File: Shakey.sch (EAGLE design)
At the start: 38 parts, among them CN1 CONN_USB-4UCON-11071, Y1 16Mhz

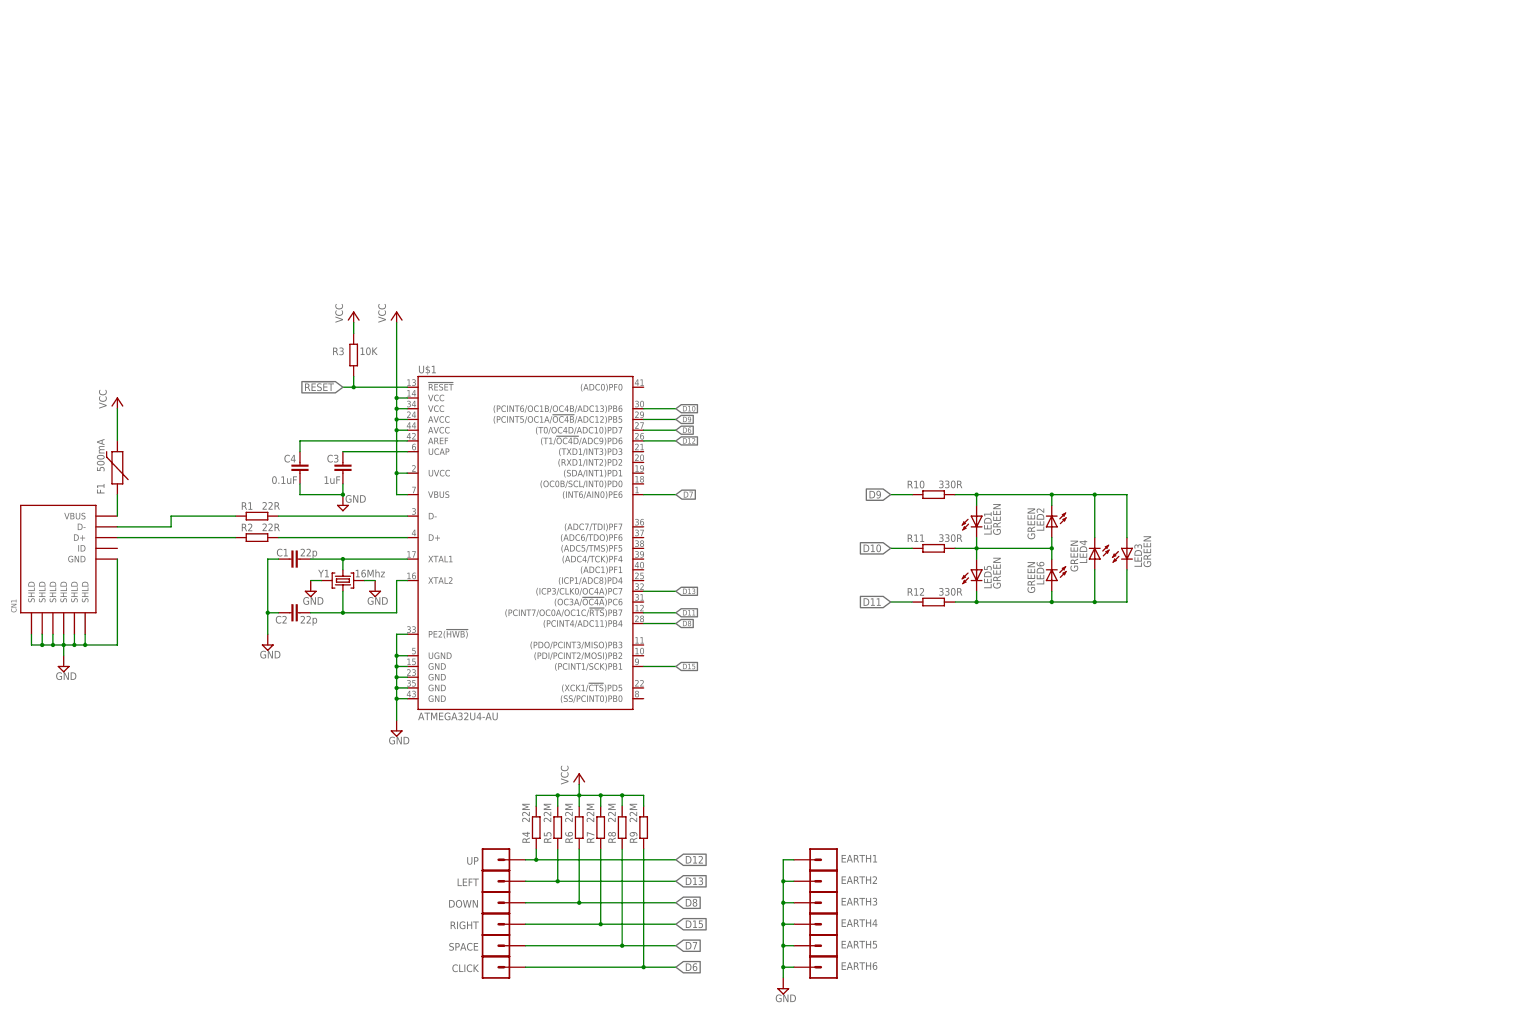
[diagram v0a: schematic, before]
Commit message: completed basic schematic
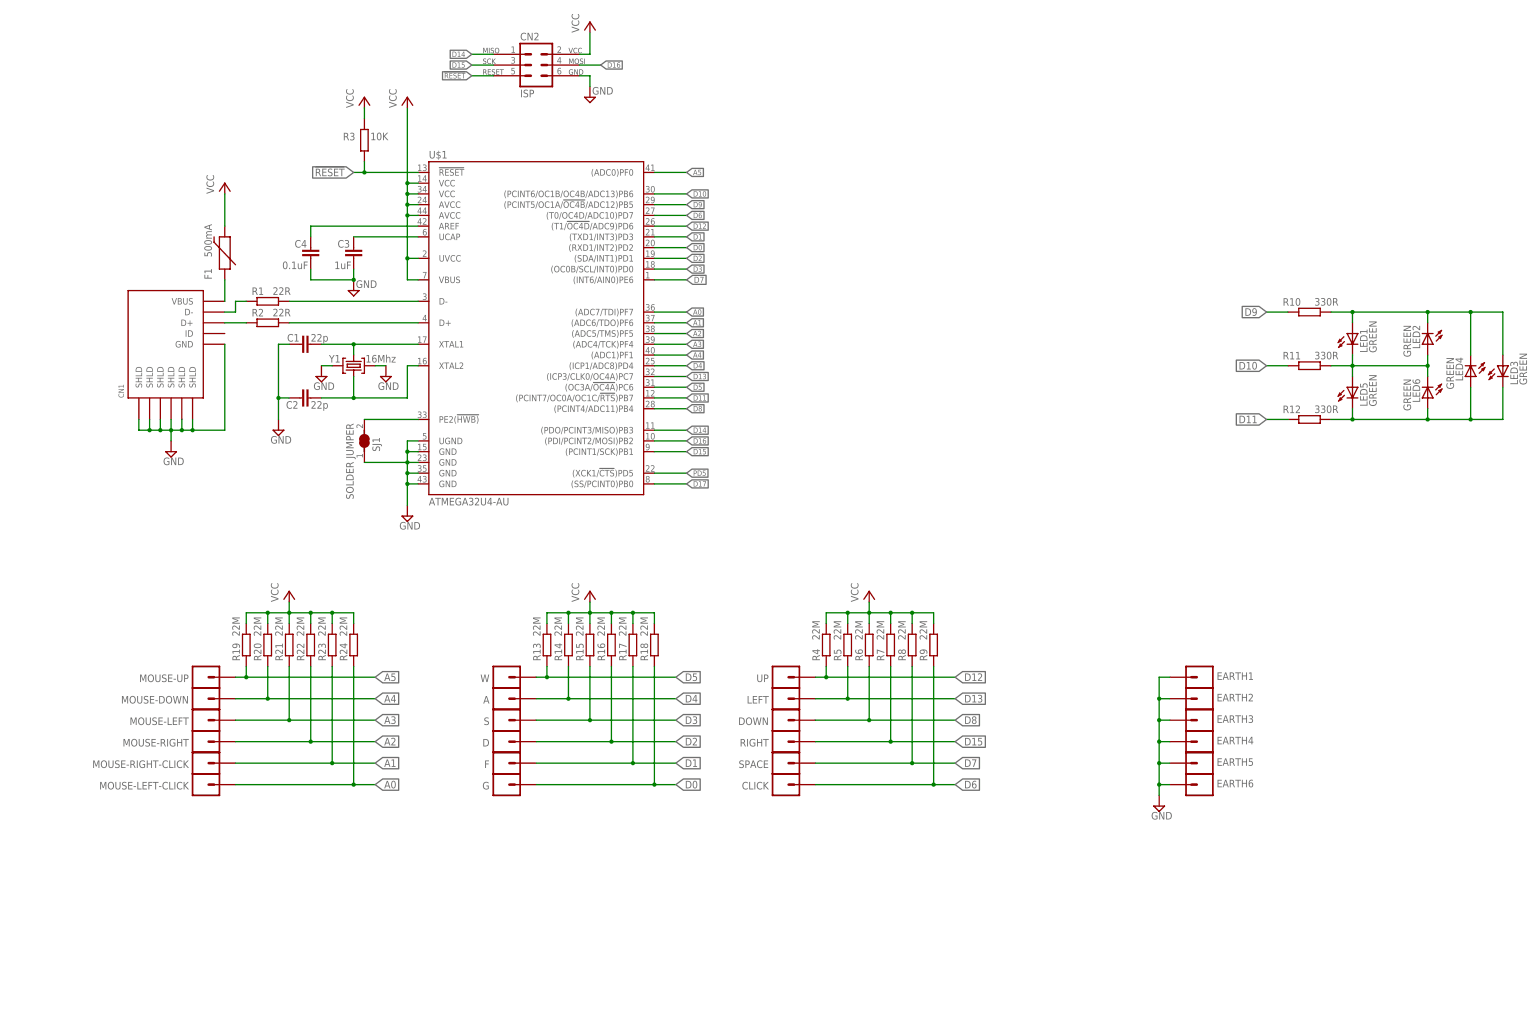
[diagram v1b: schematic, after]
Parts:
- added A, D, F, G, MOUSE-DOWN, MOUSE-LEFT, MOUSE-LEFT-CLICK, MOUSE-RIGHT, MOUSE-RIGHT-CLICK, MOUSE-UP, S, W: MA01-1-ALLIGATOR-3MM, SixthLogic:MA01-1-ALLIGATOR-3MM
- added CN2: ISP, SixthLogic:DEBUGPORT-6PIN-ISP-AVR
- added R13, R14, R15, R16, R17, R18, R19, R20, R21, R22, R23, R24: 22M, rcl:R-EU_R0603
- added SJ1: SOLDER JUMPER, SixthLogic:SOLDER_JUMPER_NC
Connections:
- new net A0: MOUSE-LEFT-CLICK.1, R24.1, U$1.(ADC7/TDI)PF7
- new net A1: MOUSE-RIGHT-CLICK.1, R23.1, U$1.(ADC6/TDO)PF6
- new net A2: MOUSE-RIGHT.1, R22.1, U$1.(ADC5/TMS)PF5
- new net A3: MOUSE-LEFT.1, R21.1, U$1.(ADC4/TCK)PF4
- new net A4: MOUSE-DOWN.1, R20.1, U$1.(ADC1)PF1
- new net A5: MOUSE-UP.1, R19.1, U$1.(ADC0)PF0
- new net D0: G.1, R18.1, U$1.(RXD1/INT2)PD2
- new net D1: F.1, R17.1, U$1.(TXD1/INT3)PD3
- new net D14: CN2.1, U$1.(PDO/PCINT3/MISO)PB3
- new net D16: CN2.4, U$1.(PDI/PCINT2/MOSI)PB2
- new net D17: U$1.(SS/PCINT0)PB0
- new net D2: D.1, R16.1, U$1.(SDA/INT1)PD1
- new net D3: R15.1, S.1, U$1.(OC0B/SCL/INT0)PD0
- new net D4: A.1, R14.1, U$1.(ICP1/ADC8)PD4
- new net D5: R13.1, U$1.(OC3A/!OC4A!)PC6, W.1
- new net N$13: SJ1.2, U$1.PE2(!HWB)
- new net PD5: U$1.(XCK1/!CTS!)PD5
- net !RESET!: now also CN2.5
- net D15: now also CN2.3
- net GND: now also CN2.6, SJ1.1; no longer U$1.PE2(!HWB)
- net VCC: now also CN2.2, R13.2, R14.2, R15.2, R16.2, R17.2, R18.2, R19.2, R20.2, R21.2, R22.2, R23.2, R24.2
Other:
- moved on the sheet: C1, C2, C3, C4, CLICK, CN1, DOWN, EARTH1, EARTH2, EARTH3, EARTH4, EARTH5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

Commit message: completed schematic
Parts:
- removed D, S: MA01-1-ALLIGATOR-3MM, SixthLogic:MA01-1-ALLIGATOR-3MM
- removed U$1: ATMEGA32U4-AU, SixthLogic:ATMEGA32U4-AU
- added C5, C8: 1uF, rcl:C-EUC0603
- added C6: 0.1uF, rcl:C-EUC0603
- added C7: 2.2uF, rcl:C-EUC0603
- added C9: 0.47uF, rcl:C-EUC0603
- added LED7, LED8: YELLOW, led:LEDCHIPLED_0603
- added LED9: RED, led:LEDCHIPLED_0603
- added PC1: 10uF, SixthLogic:CAP_POL-CT6032
- added R25, R26, R27: 1K, rcl:R-EU_R0603
- added R28, R29, R30, R31: 10K, rcl:R-EU_R0603
- added TR1, TR2: BSS138, SixthLogic:MOSFET-N-BSS138
- added U1: ATMEGA32U4-AU, SixthLogic:ATMEGA32U4-AU
- added U2: ICM-20689, SixthLogic:ICM-20689
- added U3: AP2210K-3.3TRG1, SixthLogic:AP2210K-3.3TRG1
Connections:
- removed net D17: U$1.(SS/PCINT0)PB0
- removed net D2: D.1, R16.1, U$1.(SDA/INT1)PD1
- removed net D3: R15.1, S.1, U$1.(OC0B/SCL/INT0)PD0
- removed net PD5: U$1.(XCK1/!CTS!)PD5
- new net 3.3V: C5.2, C6.2, C7.2, R28.2, R29.2, TR1.G, TR2.G, U2.NCS, U2.VDD, U2.VDDIO, U3.VOUT
- new net HWB: SJ1.2, U1.PE2(!HWB)
- new net N$17: LED7.A, R25.1
- new net N$18: LED8.A, R26.1
- new net N$19: LED9.A, R27.1
- new net RX_LED: LED8.C, U1.(SS/PCINT0)PB0
- new net SCL_HV: R31.1, TR2.D, U1.(OC0B/SCL/INT0)PD0
- new net SCL_LV: R29.1, TR2.S, U2.SCL/SCLK
- new net SDA_HV: R30.1, TR1.D, U1.(SDA/INT1)PD1
- new net SDA_LV: R28.1, TR1.S, U2.SDA/SDI
- new net TX_LED: LED7.C, U1.(XCK1/!CTS!)PD5
- net !RESET!: now also U1.!RESET; no longer U$1.!RESET
- net A0: now also U1.(ADC7/TDI)PF7; no longer U$1.(ADC7/TDI)PF7
- net A1: now also U1.(ADC6/TDO)PF6; no longer U$1.(ADC6/TDO)PF6
- net A2: now also U1.(ADC5/TMS)PF5; no longer U$1.(ADC5/TMS)PF5
- net A3: now also U1.(ADC4/TCK)PF4; no longer U$1.(ADC4/TCK)PF4
- net A4: now also U1.(ADC1)PF1; no longer U$1.(ADC1)PF1
- net A5: now also U1.(ADC0)PF0; no longer U$1.(ADC0)PF0
- net D0: now also U1.(RXD1/INT2)PD2; no longer U$1.(RXD1/INT2)PD2
- net D1: now also U1.(TXD1/INT3)PD3; no longer U$1.(TXD1/INT3)PD3
- net D10: now also U1.(PCINT6/OC1B/OC4B/ADC13)PB6; no longer U$1.(PCINT6/OC1B/OC4B/ADC13)PB6
- net D11: now also U1.(PCINT7/OC0A/OC1C/!RTS!)PB7; no longer U$1.(PCINT7/OC0A/OC1C/!RTS!)PB7
- net D12: now also U1.(T1/!OC4D!/ADC9)PD6; no longer U$1.(T1/!OC4D!/ADC9)PD6
- net D13: now also U1.(ICP3/CLK0/OC4A)PC7; no longer U$1.(ICP3/CLK0/OC4A)PC7
- net D14: now also U1.(PDO/PCINT3/MISO)PB3; no longer U$1.(PDO/PCINT3/MISO)PB3
- net D15: now also U1.(PCINT1/SCK)PB1; no longer U$1.(PCINT1/SCK)PB1
- net D16: now also U1.(PDI/PCINT2/MOSI)PB2; no longer U$1.(PDI/PCINT2/MOSI)PB2
- net D4: now also U1.(ICP1/ADC8)PD4; no longer U$1.(ICP1/ADC8)PD4
- net D5: now also U1.(OC3A/!OC4A!)PC6; no longer U$1.(OC3A/!OC4A!)PC6
- net D6: now also U1.(T0/OC4D/ADC10)PD7; no longer U$1.(T0/OC4D/ADC10)PD7
- net D7: now also U1.(INT6/AIN0)PE6; no longer U$1.(INT6/AIN0)PE6
- net D8: now also U1.(PCINT4/ADC11)PB4; no longer U$1.(PCINT4/ADC11)PB4
- net D9: now also U1.(PCINT5/OC1A/!OC4B!/ADC12)PB5; no longer U$1.(PCINT5/OC1A/!OC4B!/ADC12)PB5
- net GND: now also C5.1, C6.1, C7.1, C8.1, C9.1, LED9.C, PC1.-, U1.GND@15, U1.GND@23, U1.GND@35, U1.GND@43, U1.UGND, U2.AD0/SDO, U2.EPX_PAD, U2.FSYNC, U2.GND, U3.GND; no longer U$1.GND@15, U$1.GND@23, U$1.GND@35, U$1.GND@43, U$1.UGND
- net N$1: now also U1.AREF; no longer U$1.AREF
- net N$13: now also C9.2, U2.REGOUT; no longer SJ1.2, U$1.PE2(!HWB)
- net N$2: now also U1.XTAL1; no longer U$1.XTAL1
- net N$3: now also U1.XTAL2; no longer U$1.XTAL2
- net N$6: now also U1.UCAP; no longer U$1.UCAP
- net N$8: now also U1.D-; no longer U$1.D-
- net N$9: now also U1.D+; no longer U$1.D+
- net VCC: now also C8.2, PC1.+, R25.2, R26.2, R27.2, R30.2, R31.2, U1.AVCC@24, U1.AVCC@44, U1.UVCC, U1.VBUS, U1.VCC@14, U1.VCC@34, U3.EN, U3.VIN; no longer U$1.AVCC@24, U$1.AVCC@44, U$1.UVCC, U$1.VBUS, U$1.VCC@14, U$1.VCC@34
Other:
- moved on the sheet: A, C1, C2, C3, C4, CLICK, CN1, CN2, DOWN, EARTH1, EARTH2, EARTH3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

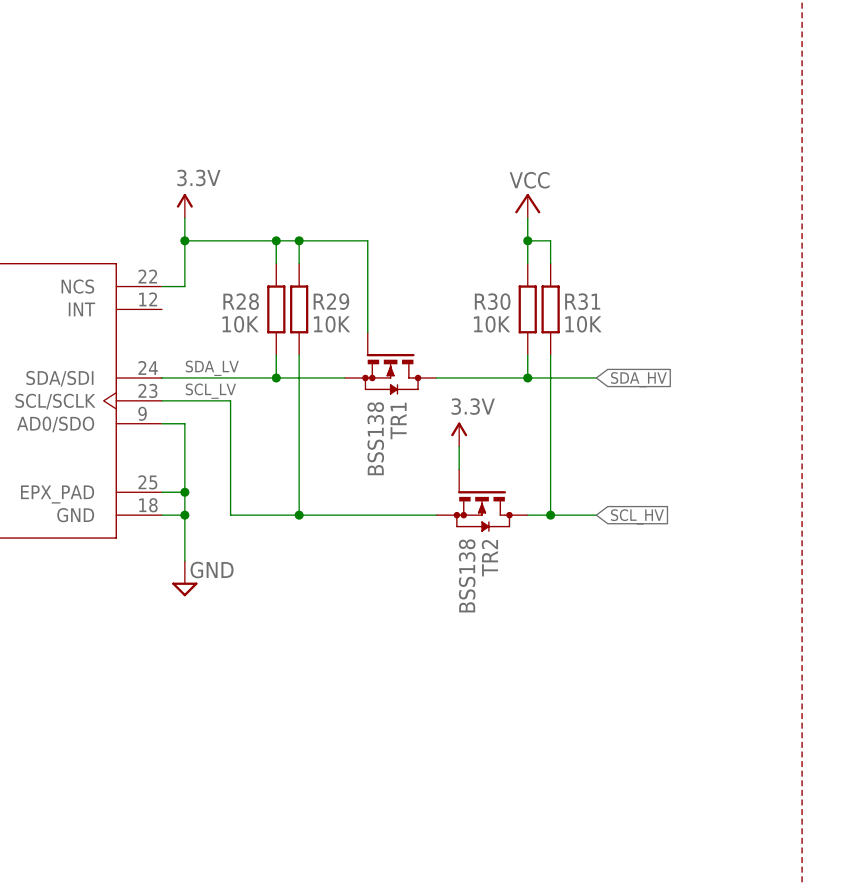
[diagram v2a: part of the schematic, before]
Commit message: rearranged level shifter
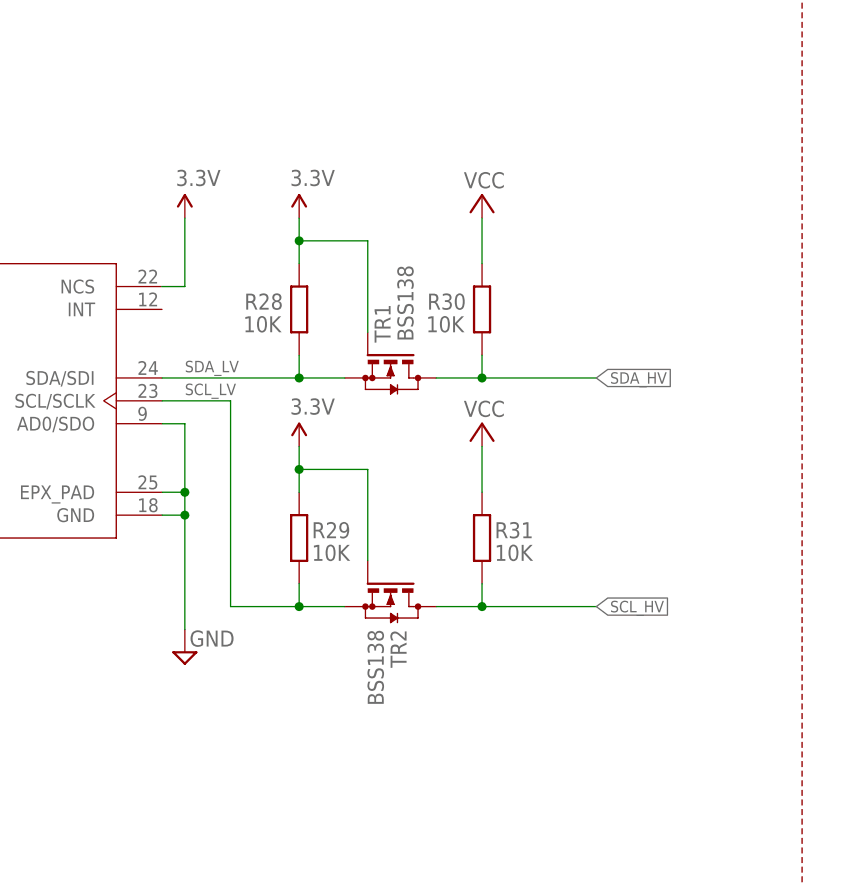
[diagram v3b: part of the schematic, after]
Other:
- moved on the sheet: R28, R29, R30, R31, TR2
